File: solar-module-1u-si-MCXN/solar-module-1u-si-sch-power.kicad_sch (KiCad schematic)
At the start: 61 parts, among them J1 MMS-104-01-[F/L]-SH, Q1 NTR4101P, Q2 DMP2240UDM-7, U10 TPS63060DSCR, U12 LTC4412, U3 LT1618EMSTRPBF, U4 INA226

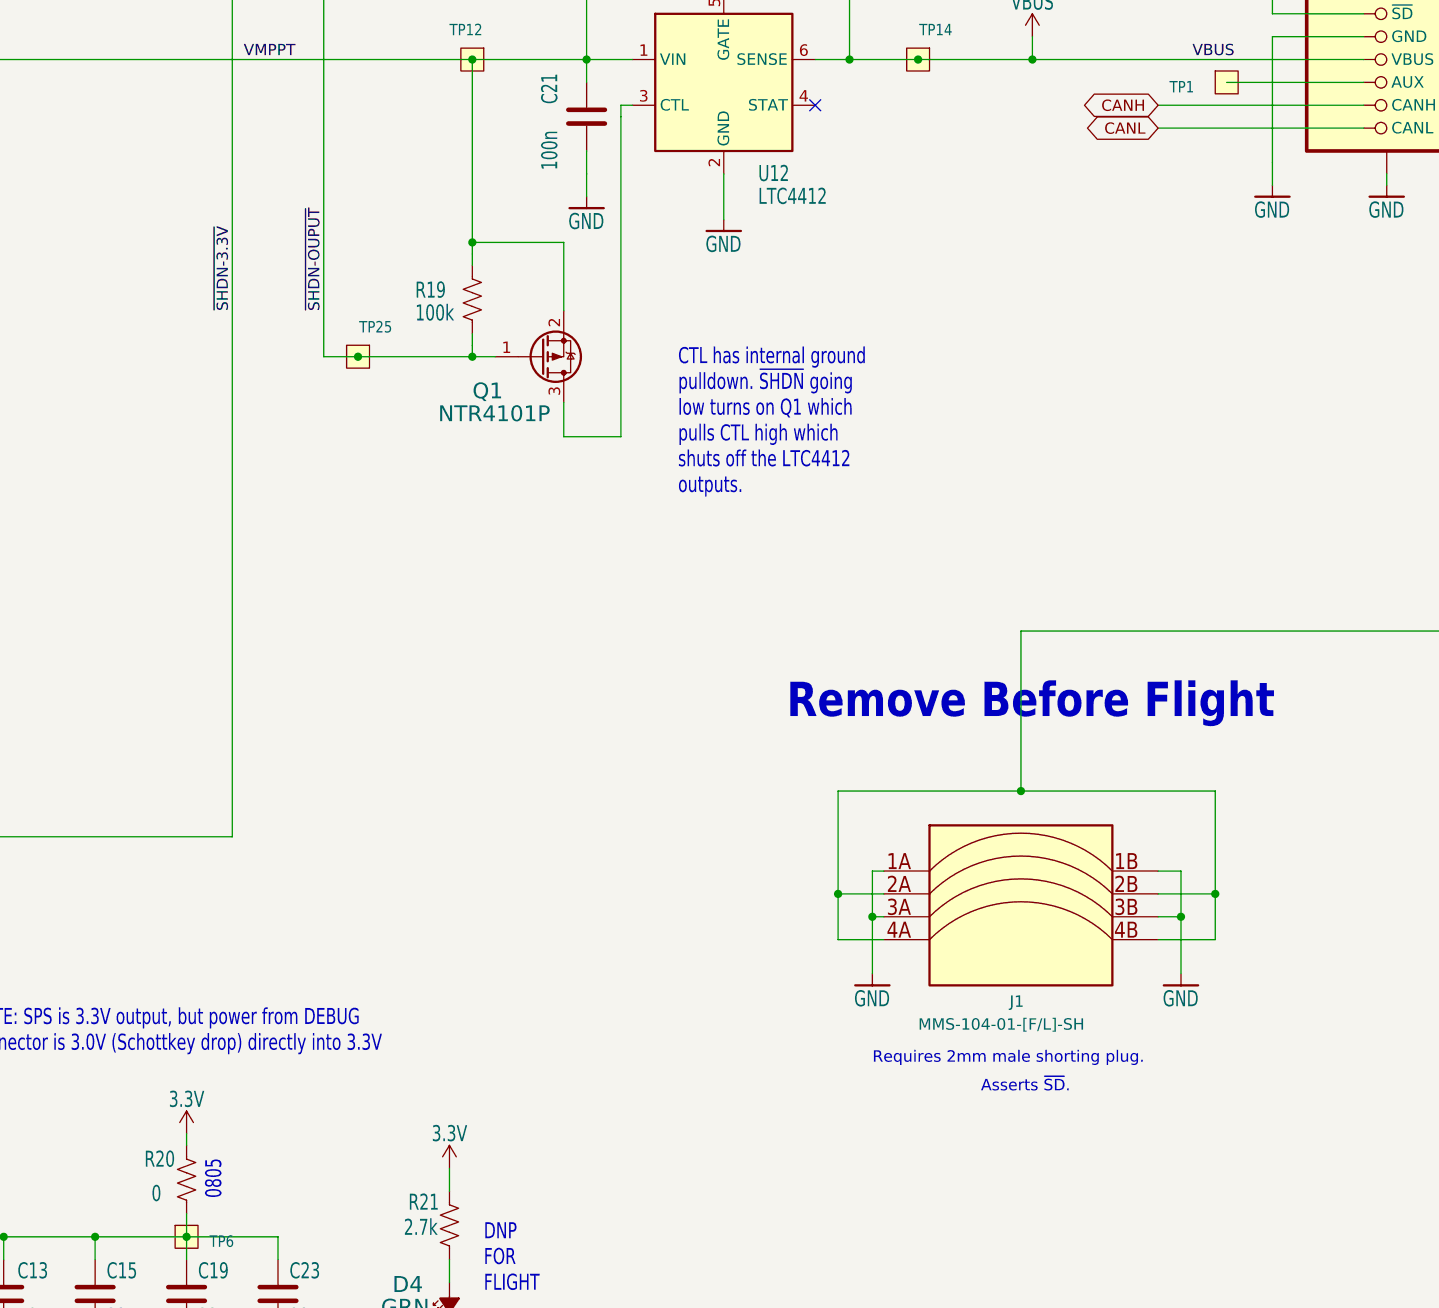
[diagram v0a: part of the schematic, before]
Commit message: Fixed ERC errors, including unused blocks and some power stuff.
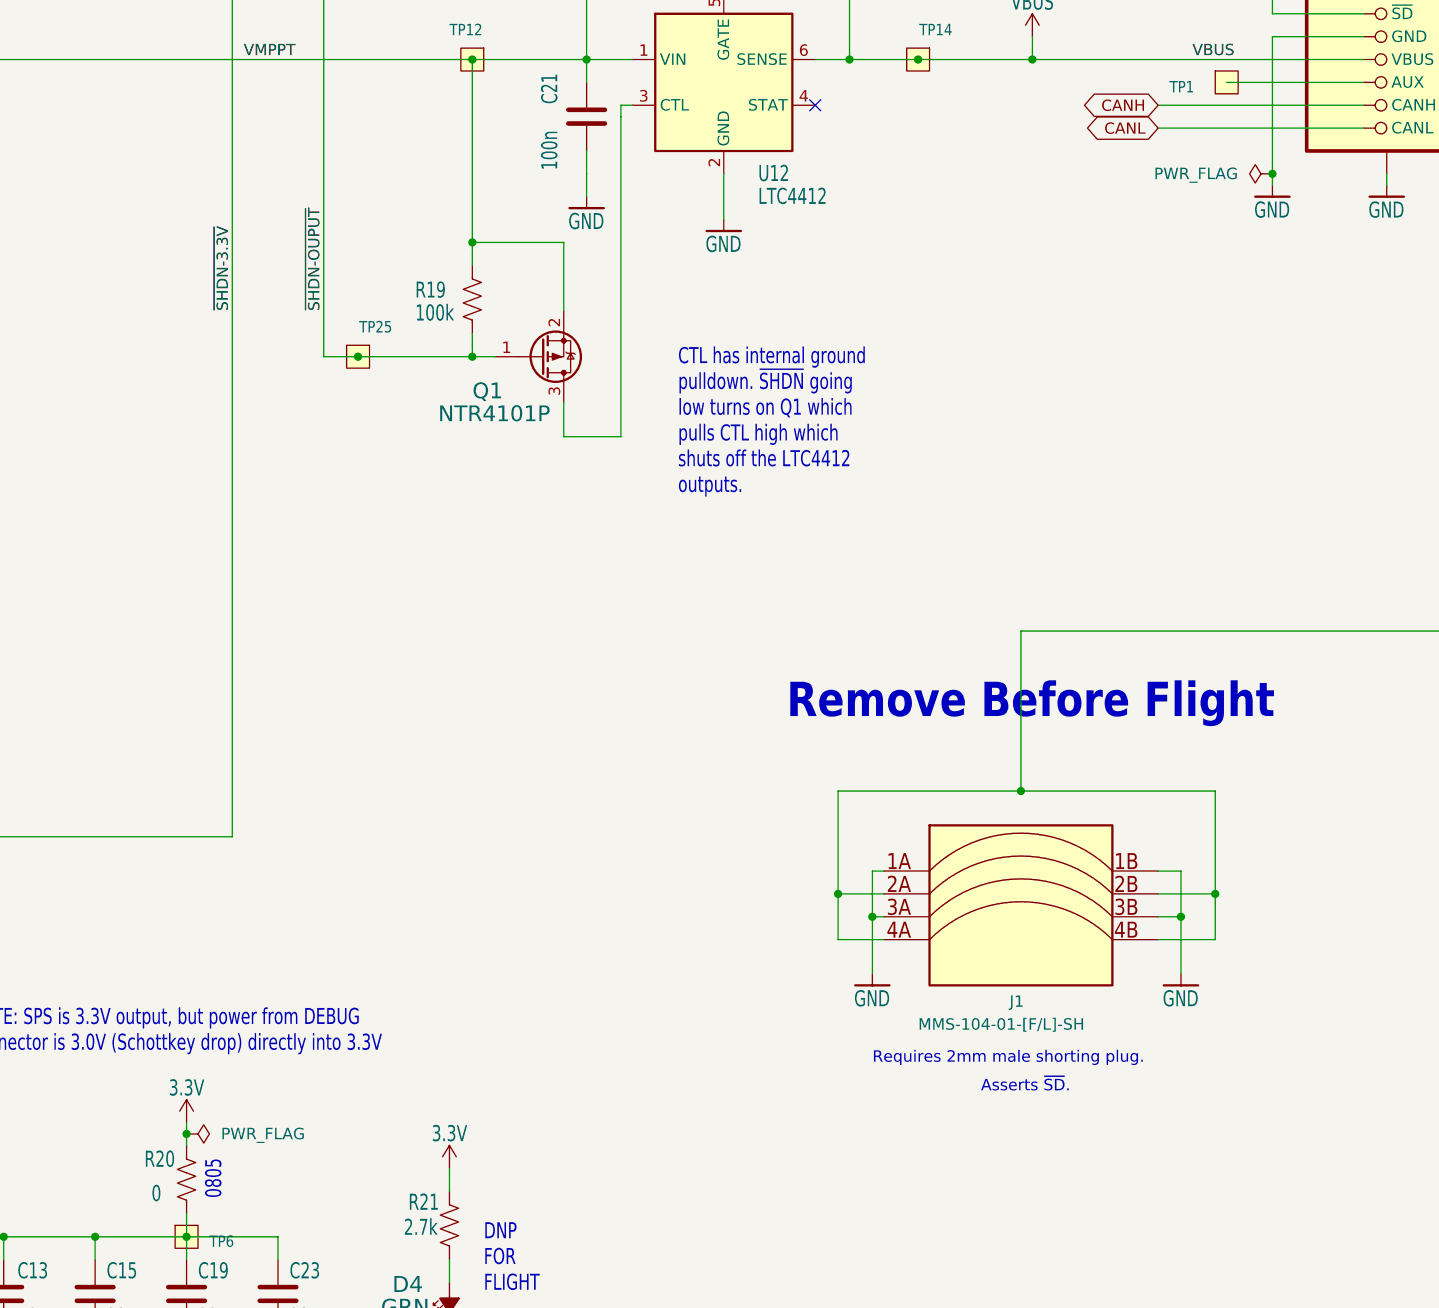
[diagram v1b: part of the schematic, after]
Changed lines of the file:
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@@
 	)
 	(junction
+		(at 246.38 179.07)
+		(diameter 0)
+		(color 0 0 0 0)
+	)
+	(junction
 		(at 147.32 86.36)
 		(diameter 0)
@@
 	)
 	(junction
+		(at 367.03 72.39)
+		(diameter 0)
+		(color 0 0 0 0)
+	)
+	(junction
 		(at 207.01 190.5)
 		(diameter 0)
@@
 	(wire
 		(pts
+			(xy 246.38 177.8) (xy 246.38 179.07)
+		)
+		(stroke
+			(width 0)
+			(type default)
+		)
+	)
+	(wire
+		(pts
 			(xy 147.32 87.63) (xy 147.32 86.36)
 		)
@@
 	(wire
 		(pts
+			(xy 367.03 72.39) (xy 367.03 73.66)
+		)
+		(stroke
+			(width 0)
+			(type default)
+		)
+	)
+	(wire
+		(pts
 			(xy 59.69 88.9) (xy 60.96 88.9)
 		)
@@
 	(wire
 		(pts
-			(xy 367.03 71.12) (xy 367.03 73.66)
+			(xy 367.03 71.12) (xy 367.03 72.39)
 		)
 		(stroke
@@
 	)
 	(symbol
+		(lib_id "power:PWR_FLAG")
+		(at 246.38 179.07 270)
+		(unit 1)
+		(exclude_from_sim no)
+		(in_bom yes)
+		(on_board yes)
+		(dnp no)
+		(fields_autoplaced yes)
+		(property "Reference" "#FLG01"
+			(at 248.285 179.07 0)
+			(effects
+				(font
+					(size 1.27 1.27)
+				)
+				(hide yes)
+			)
+		)
+		(property "Value" "PWR_FLAG"
+			(at 250.19 179.0699 90)
+			(effects
+				(font
+					(size 1.27 1.27)
+				)
+				(justify left)
+			)
+		)
+		(property "Footprint" ""
+			(at 246.38 179.07 0)
+			(effects
+				(font
+					(size 1.27 1.27)
+				)
+				(hide yes)
+			)
+		)
+		(property "Datasheet" "~"
+			(at 246.38 179.07 0)
+			(effects
+				(font
+					(size 1.27 1.27)
+				)
+				(hide yes)
+			)
+		)
+		(property "Description" "Special symbol for telling ERC where power comes from"
+			(at 246.38 179.07 0)
+			(effects
+				(font
+					(size 1.27 1.27)
+				)
+				(hide yes)
+			)
+		)
+		(pin "1"
+		)
+		(instances
+			(project ""
+				(path "/115bd2cd-7c08-4b54-867b-a326ee0699c1/5c4415f1-d90e-44ce-bb2c-b4c8edead48f"
+					(reference "#FLG01")
+					(unit 1)
+				)
+			)
+		)
+	)
+	(symbol
 		(lib_id "oresat-power:3.3V")
-		(at 246.38 179.07 0)
+		(at 246.38 177.8 0)
 		(unit 1)
 		(exclude_from_sim no)
@@
 		(dnp no)
 		(property "Reference" "#SUPPLY01"
-			(at 246.38 179.07 0)
+			(at 246.38 177.8 0)
 			(effects
 				(font
@@
 		)
 		(property "Value" "3.3V"
-			(at 246.38 176.276 0)
+			(at 246.38 175.006 0)
 			(effects
 				(font
@@
 		)
 		(property "Footprint" ""
-			(at 246.38 179.07 0)
+			(at 246.38 177.8 0)
 			(effects
 				(font
@@
 		)
 		(property "Datasheet" ""
-			(at 246.38 179.07 0)
+			(at 246.38 177.8 0)
 			(effects
 				(font
@@
 		)
 		(property "Description" "Power symbol creates a global label with name \"3.3V\""
-			(at 246.38 179.07 0)
+			(at 246.38 177.8 0)
 			(effects
 				(font
@@
 					(unit 1)
 				)
+			)
+		)
+	)
+	(symbol
+		(lib_id "power:PWR_FLAG")
+		(at 367.03 72.39 90)
+		(mirror x)
+		(unit 1)
+		(exclude_from_sim no)
+		(in_bom yes)
+		(on_board yes)
+		(dnp no)
+		(property "Reference" "#FLG02"
+			(at 365.125 72.39 0)
+			(effects
+				(font
+					(size 1.27 1.27)
+				)
+				(hide yes)
+			)
+		)
+		(property "Value" "PWR_FLAG"
+			(at 363.22 72.3899 90)
+			(effects
+				(font
+					(size 1.27 1.27)
+				)
+				(justify left)
+			)
+		)
+		(property "Footprint" ""
+			(at 367.03 72.39 0)
+			(effects
+				(font
+					(size 1.27 1.27)
+				)
+				(hide yes)
+			)
+		)
+		(property "Datasheet" "~"
+			(at 367.03 72.39 0)
+			(effects
+				(font
+					(size 1.27 1.27)
+				)
+				(hide yes)
+			)
+		)
+		(property "Description" "Special symbol for telling ERC where power comes from"
+			(at 367.03 72.39 0)
+			(effects
+				(font
+					(size 1.27 1.27)
+				)
+				(hide yes)
+			)
+		)
+		(pin "1"
+		)
+		(instances
+			(project "solar-module-1u-si"
+				(path "/115bd2cd-7c08-4b54-867b-a326ee0699c1/5c4415f1-d90e-44ce-bb2c-b4c8edead48f"
+					(reference "#FLG02")
+					(unit 1)
+				)

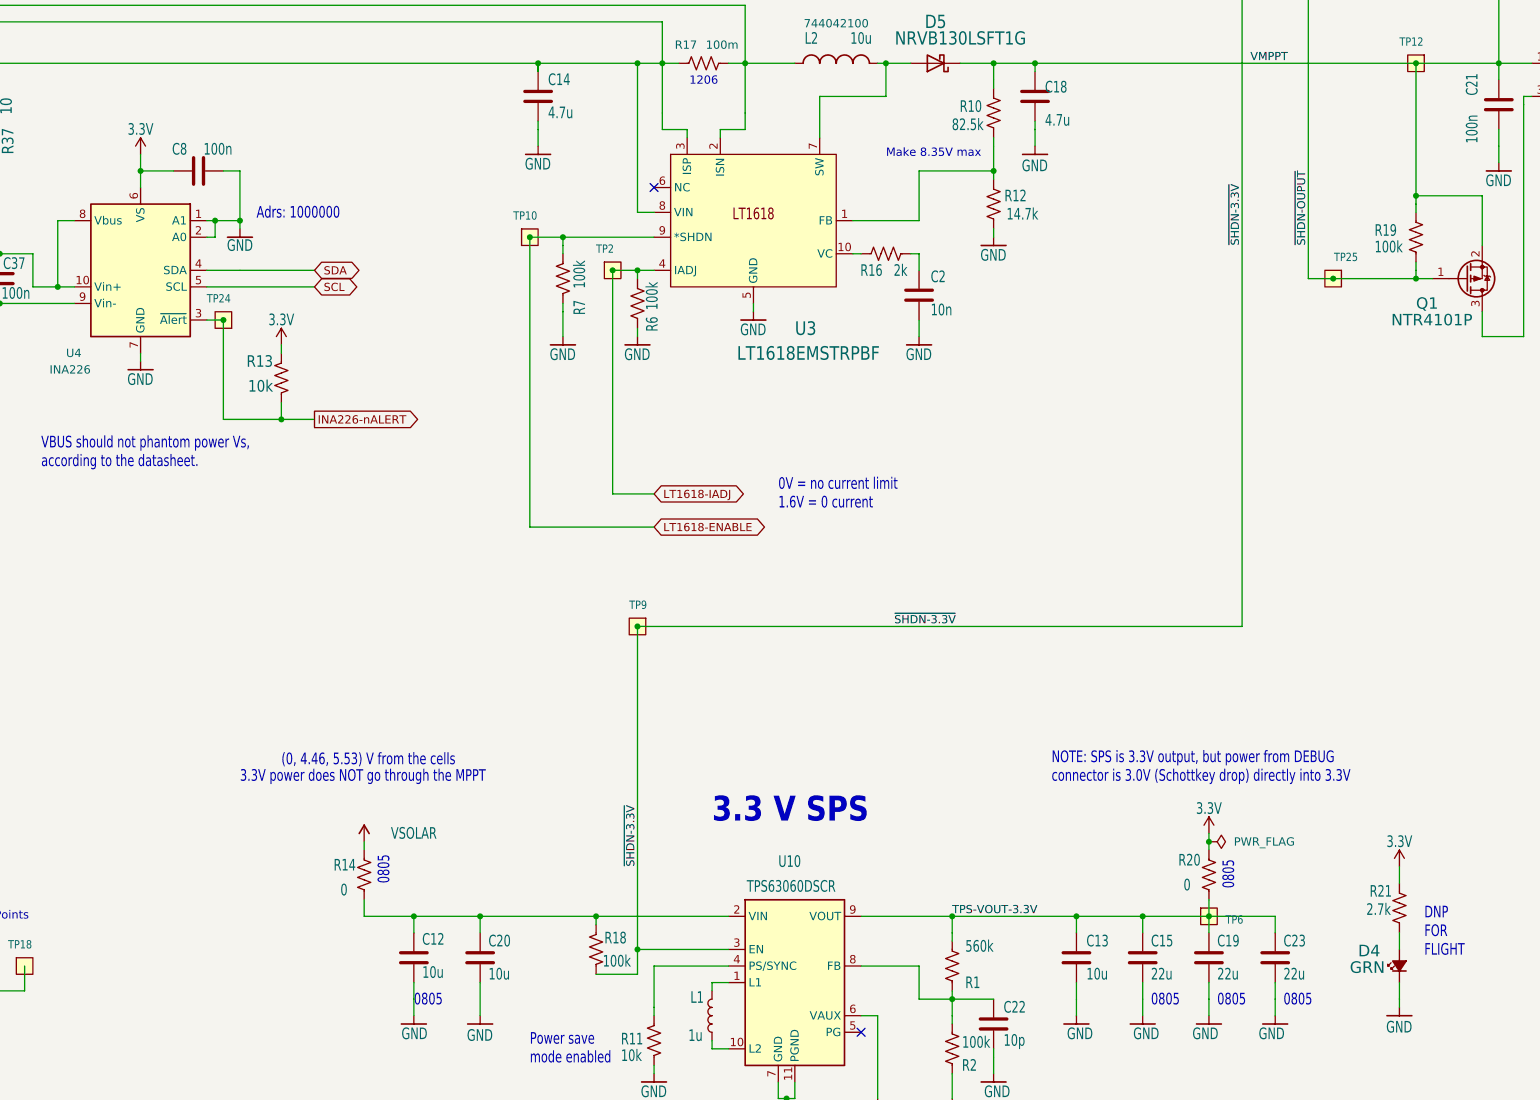
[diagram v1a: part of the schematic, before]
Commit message: moved to 4 layer board and added MCXN to PCB, some routing started
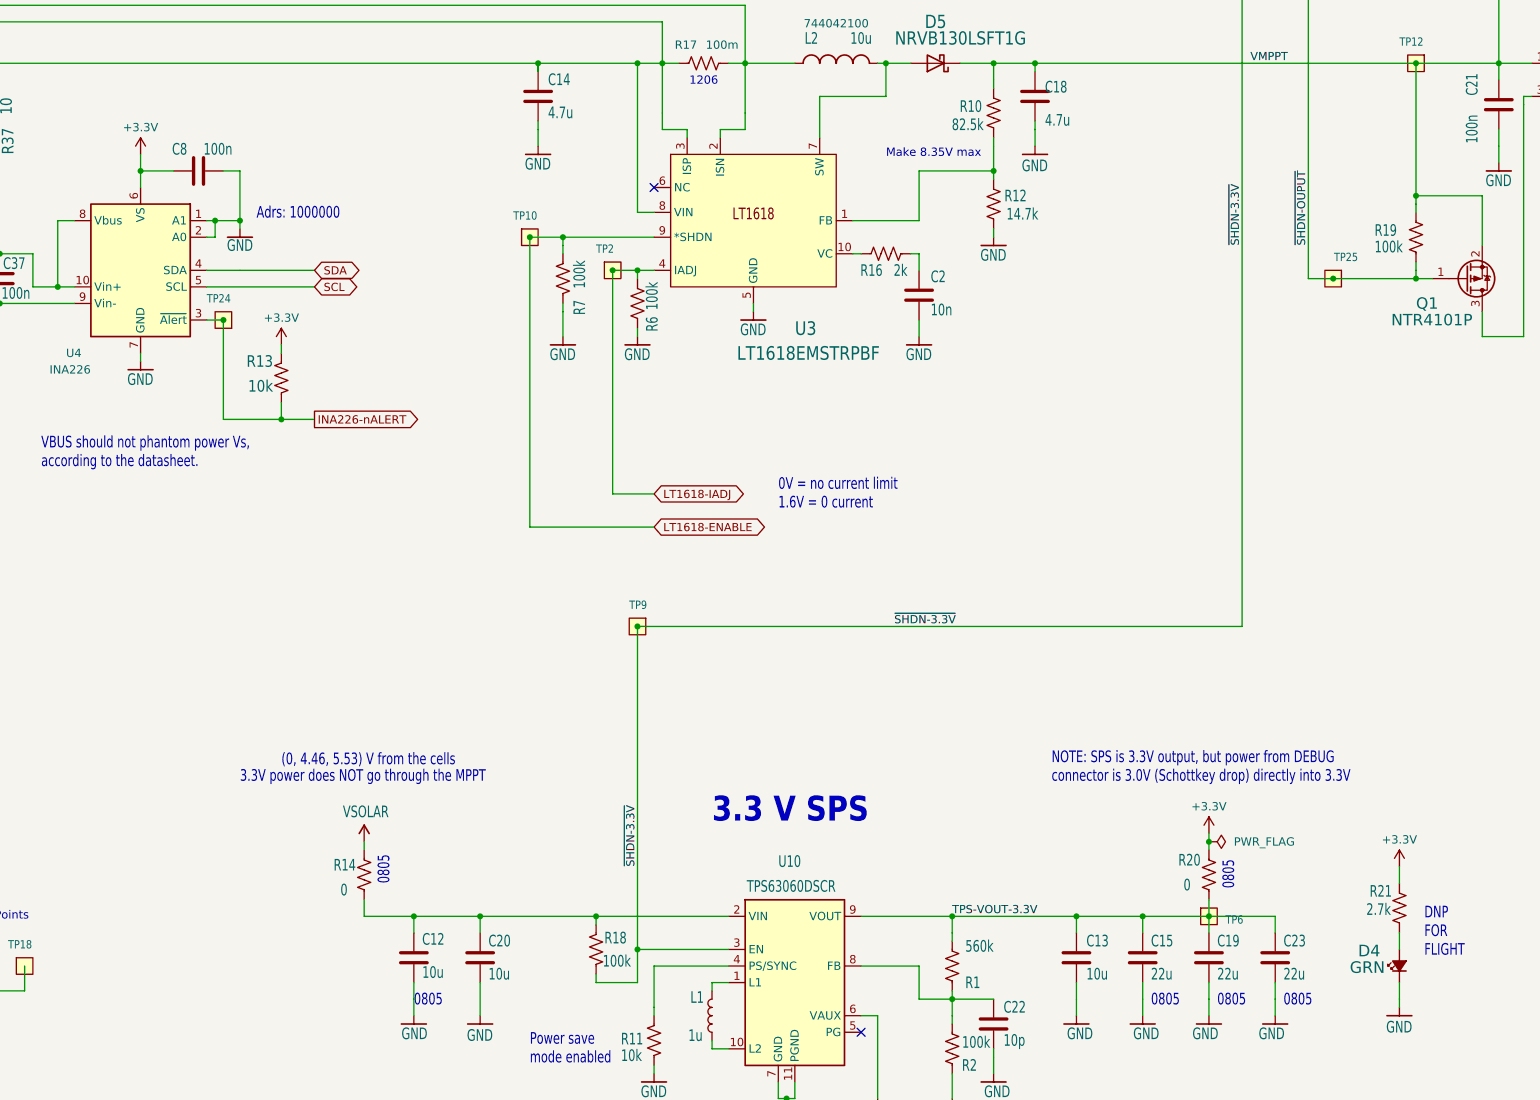
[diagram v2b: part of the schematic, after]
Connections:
- net 3.3V renamed +3.3V

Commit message: D1 and D3 footprints updated, moved debug connector, added additional power vias, moved temp sensors from screw holes, fixed silkscreen
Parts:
- D1, D3: footprint oresat-diodes:D-SOD323-R -> Diode_SMD:D_SOD-323F
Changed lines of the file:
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@@
 			)
 		)
-		(property "Footprint" "oresat-diodes:D-SOD323-R"
+		(property "Footprint" "Diode_SMD:D_SOD-323F"
 			(at 261.62 43.18 0)
 			(effects
@@
 			)
 		)
-		(property "Footprint" "oresat-diodes:D-SOD323-R"
+		(property "Footprint" "Diode_SMD:D_SOD-323F"
 			(at 251.46 43.18 0)
 			(effects
